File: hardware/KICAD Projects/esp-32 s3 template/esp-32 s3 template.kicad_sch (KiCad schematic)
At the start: 39 parts, among them J1 TYPE-C-31-M-12, J2 DTF13-6P, SW1 PTS810_SJM_250_SMTR_LFS, SW2 PTS810_SJM_250_SMTR_LFS, U1 AMS1117-3.3, U2 ESP32-S3-WROOM-1, U3 MCP2515-I, U4 TJA1050DRG, X1 ${ALTIUM_VALUE}

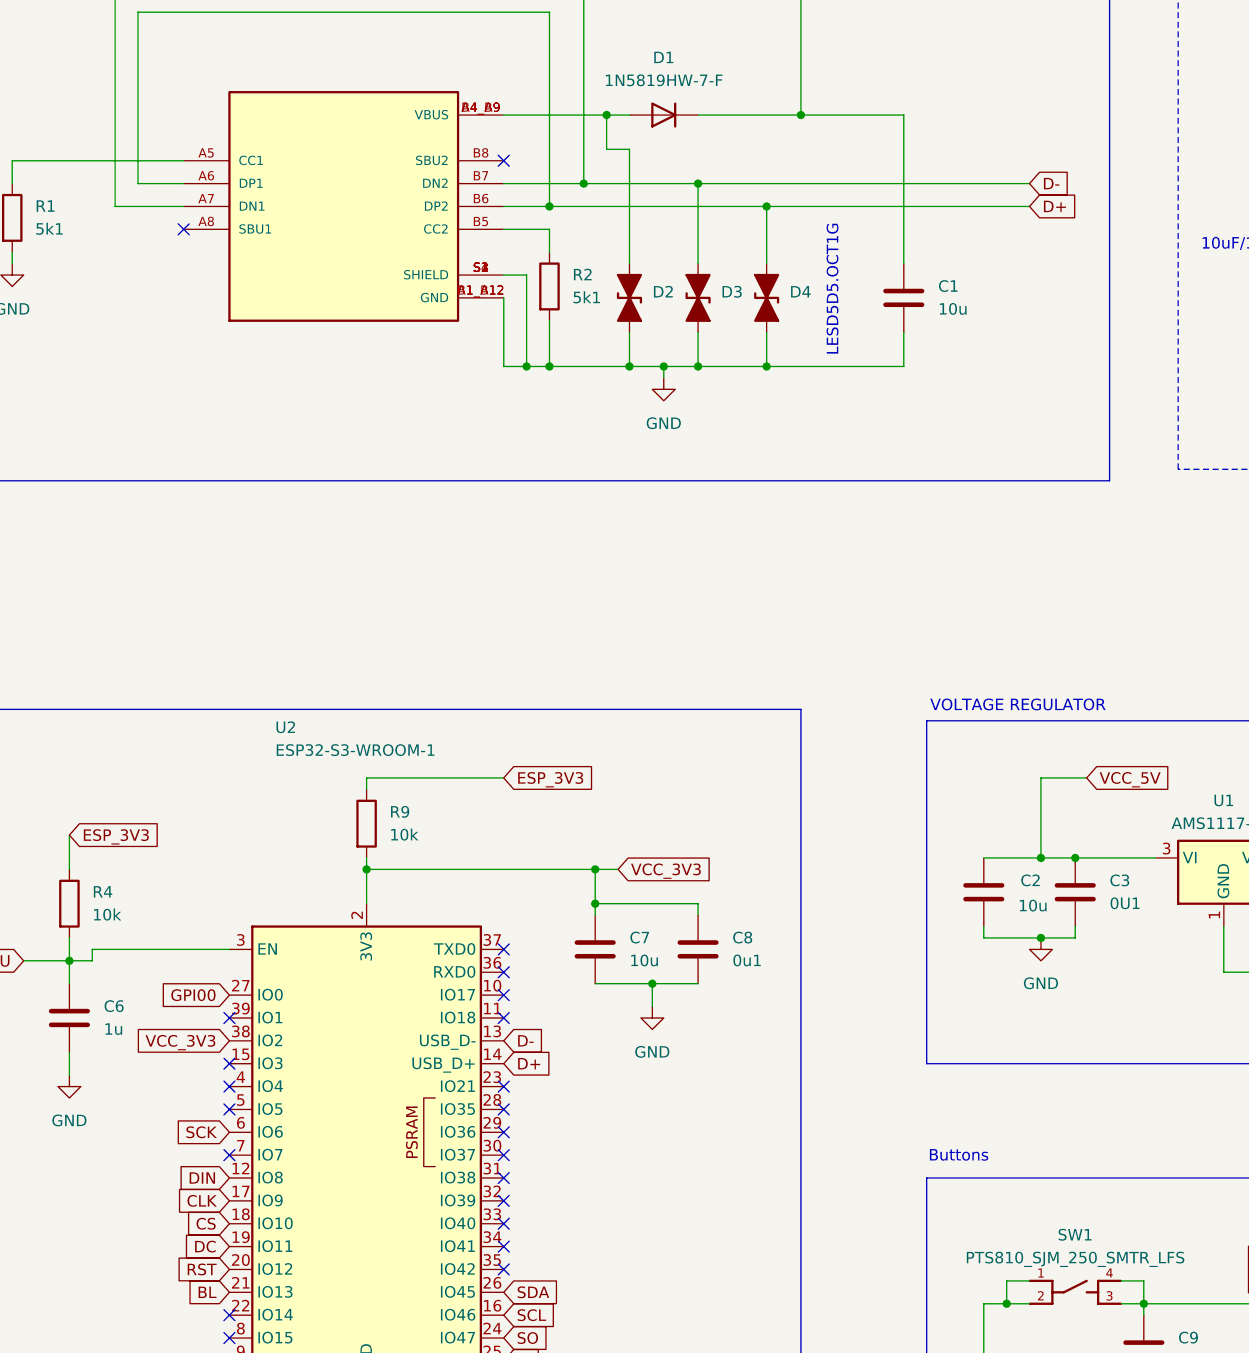
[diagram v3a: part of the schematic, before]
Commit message: everything but the ground fill
done, having some trouble with the ground fills
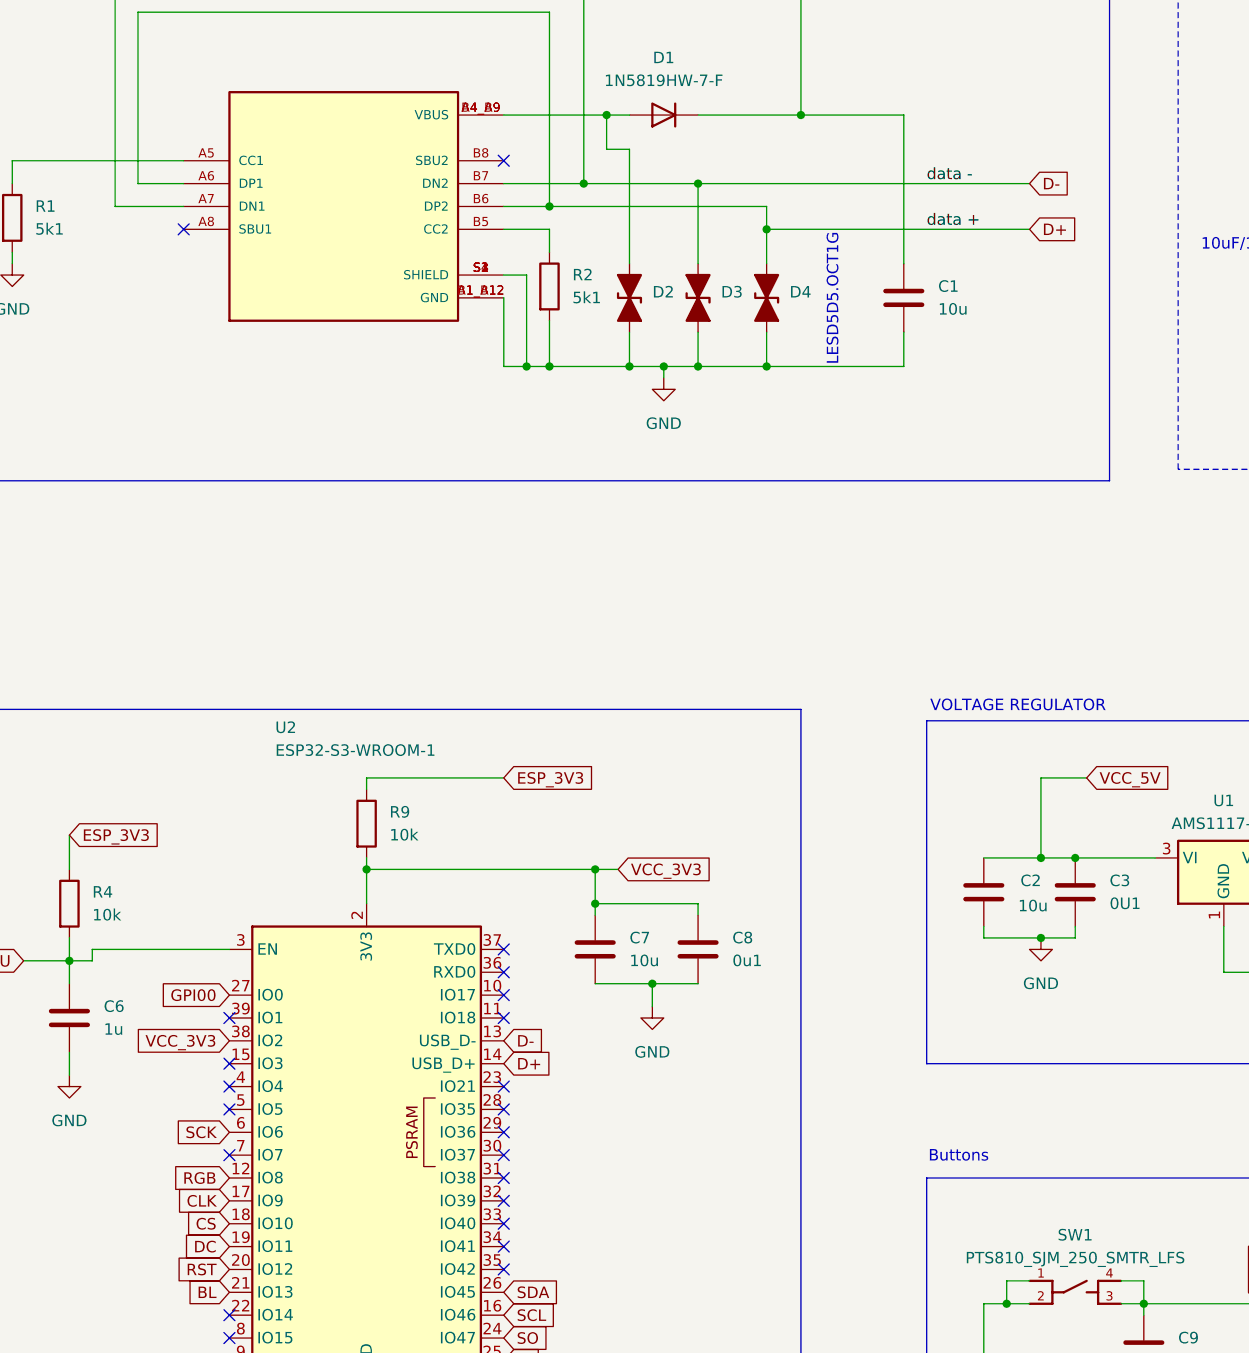
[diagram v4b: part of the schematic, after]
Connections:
- net DIN is gone; now on net RGB: U2.12 (IO8)
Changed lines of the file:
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@@
 	(text "LESD5D5.OCT1G"
 		(exclude_from_sim no)
-		(at 149.606 79.248 90)
+		(at 149.606 80.264 90)
 		(effects
 			(font
@@
 	)
 	(junction
-		(at 142.24 69.85)
-		(diameter 0)
-		(color 0 0 0 0)
-	)
-	(junction
 		(at 121.92 67.31)
 		(diameter 0)
@@
 	)
 	(junction
+		(at 142.24 72.39)
+		(diameter 0)
+		(color 0 0 0 0)
+	)
+	(junction
 		(at 123.19 147.32)
 		(diameter 0)
@@
 	(wire
 		(pts
-			(xy 142.24 69.85) (xy 171.45 69.85)
+			(xy 142.24 72.39) (xy 171.45 72.39)
 		)
 		(stroke
@@
 	(wire
 		(pts
+			(xy 142.24 72.39) (xy 142.24 76.2)
+		)
+		(stroke
+			(width 0)
+			(type default)
+		)
+	)
+	(wire
+		(pts
 			(xy 228.6 189.23) (xy 226.06 189.23)
 		)
@@
 	(wire
 		(pts
+			(xy 142.24 72.39) (xy 142.24 69.85)
+		)
+		(stroke
+			(width 0)
+			(type default)
+		)
+	)
+	(wire
+		(pts
 			(xy 113.03 69.85) (xy 118.11 69.85)
 		)
@@
 	(wire
 		(pts
-			(xy 142.24 69.85) (xy 142.24 76.2)
-		)
-		(stroke
-			(width 0)
-			(type default)
-		)
-	)
-	(wire
-		(pts
 			(xy 294.64 86.36) (xy 294.64 77.47)
 		)
@@
 			"MwA0ADkARQAtADMAMABDADMALQA0AEYAMQA1AC0AOQAxADIARgAtADEANwA0AEUARAA2AEUAMABD"
 			"ADYARQBGAIJIARj//////////4JTA08RIAAAAAAAAAAAAAAAAAAAAAAAAAAAAAAAAAAAAAAAAAAA"
+			"AAAAAAAAAAAAAAAAAAAAAAAAAAAAAAAAAAAAAAAAAAAAAAAAAAQAAG8BAAAAAAAAAAAAAAAAAAAA"
+			"AAAAAAAAAAAAAACDAAAAGAEAAPUDAABnAQAAAAAAAAAAAAAAAAAAAAAAAAAAAAAAAAAAAAAAAAAA"
+			"AAAAAAAAAAAAAAAAAAAAAAAAAAAAAAAAAAAAAAAAAAAAAAAAAAAAAAAAYAAAAAoBAAAAAAAAAAAA"
+			"AAAAAAAAAAAAAAAAAAAAAAAAAAAAAAAAAAAAAAAAAAAAAAAAAAAAAAAAAAAAAAAAAAAAAAAAAAAA"
+			"AAAAAAAAAAAAAAAAAAAAAIMDAABWAQAAAAAAAAAAAAA5AAAAewAAAAAAAAAAAAAAAAAAAAAAAAAA"
+			"AAAAAAAAAAAAAAAAAAAAAAAAAAAAAAAAAAAAAAAAAAAAAAAAAAAAAAAAAAAAAAAAAAAAAAAAAAAA"
+			"AAAAAAAAAAAAAAAAAAAAAAAAAAAAAAAAAAAAAAAAAAAAAAAAAAAAAAAAAAAAAAAAAAAAAAAAAAAA"
+			"AAAAAAAAAAAAAAAAAAAAAAAAAAAAAAAAAAAAAAAAAAAAAAAAAAAAAAAAAAAAAAAAAAAAAAAAAAAA"
+			"AAAAABkAAAAoAAAAAAAAAAAAAAAAAAAAAAAAAAAAAAAAAAAAAAAAAAAAAAAAAAAAAAAAAAAAAAAA"
+			"AAAAAAAAAAAAAAAAAAAAAAAAAAAAAAAAAAAAAAAAAAAAAAAAAAAAAAAAAAAAAAAAAAAAAAAAAAAA"
+			"AAAAAAAAAAAAAAAAAAAAAAAAAAAAAAAAAAAAAAAAAAAAAAAAAAAAAAAAAAAAAAAAAAAAAAAAAAAA"
+			"AAAAAAAAAAAAAAAAAAAAAAAAAAAAAAAAAAAAAAAAAAAAAAAAAAAAAAAAAAAAAAAAAA8BAAAnAQAA"
+			"AAAAAAAAAAAAAAAAAAAAAAAAAAAAAAAAAAAAAAAAAAAAAAAAAAAAAAAAAAAAAAAAAAAAAAAAAAAA"
+			"AAAAAAAAAAAAAAAAAAAAAAAAAAAAAAAAAAAAAAAAAAAAAAAAAAAAAAAAAAAAAAAAAAAAAAAAAAAA"
+			"AAAAAAAAIQAAAD0AAAAAAAAAAAAAAAAAAAAAAAAAAAAAAAAAAAAAAAAAAAAAAAAAAAAAAAAAAAAA"
+			"AAAAAAAAAAAAAAAAAAAAAAAAAAAAAAAAAAAAAAAAAAAAAAAAAAAAAAAAAAAAAAAAAAAAAAAAAAAA"
+			"AAAAAAAAAAAAAAAAPwQAAG4BAAAAAAAAAAAAAAAAAAAAAAAAAAAAAAAAAAAAAAAAAAAAAAAAAAAA"
+			"AAAAAAAAAAAAAAAAAAAAAAAAAAAAAAAAAAAAAAAAAAAAAAAAAAAAAAAAAAAAAAAAAAAAAAAAAAAA"
+			"AAAAAAAAAAAAAAAAAAAAAAAAAAAAAAAAAAAAAAAAAAAAALQAAAAAAAAAAAAAAAAAAAAAAAAAAAAA"
+			"AAAAAAAAAAAAAAAAAAAAAAAAAAAAAAAAAAAAAAAAAAAAAAAAAAAAAAAAAAAAAAAAAAAAAAAAAAAA"
+			"AAAAAAAAAAAAAAAAAAAAAAAAAAAAAAAAAAAAAAAAAAAAAAAAAAAAAAAAAAAAAAAAAAAAAAAAAAAA"
+			"AAAAAAAAAAAAAAAAAAAAAAAAAAAAAAAAAAAAAAAAAAAAAAAAAAAAAAAAAAAAAAAAAAAAAAAAAAAA"
+			"AAAAAAAAAAAAAAAAAAAAAAAAAAAAAAAAAAAAAAAAAAAAAAAAAAAAAAAAAAAAAAAAAAAAAAAAAAAA"
+			"AAAAAAAAAAAAAAAAAAAAAAAAAAAAAAAAAAAAAAAAAAAAAAAAAAAAAAAAAAAAAAAAAAAAAAAAAAAA"
+			"AAAAAAAAAAAAAAAAAAAAAAAAAAAAAAAAAAAAAAAAAAAAAAAAAAAAAAAAAAAAAAAAAAAAAAAAAAAA"
+			"AAAAAAAAAAAAAAAAAAAAAAAAAAAAAAAAAAAAAAAAAAAAAAAAAAAAAAAAAAAAAAAAAAAAAAAAAAAA"
+			"AAAAAAAAAAAAAAAAAAAAAAAAAAAAAAAAAAAAAAAAAAAAAAAAAAAAAAAAAAAAAAAAAAAAAAAAAAAA"
+			"AAAAAAAAAAAAAAAAAAAAAAAAAAAAAAAAAAAAAAAAAAAAAAAAAAAAAAAAAAAAAAAAAAAAAAAAAAAA"
+			"AAAAAAAAAAAAAAAAAAAAAAAAAAAAAAAAAAAAAAAAAAAAAAAAAAAAAAAAAAAAAAAAAAAAAAAAAAAA"
+			"AAAAAAAAAAAAAAAAAAAAAAAAAAAAAAAAAAAAAAAAAAAAAAAAAAAAAAAAAAAAAAAAAAAAAAAAAAAA"
+			"AAAAAAAAAAAAAAAAAAAAAAAAAAAAAAAAAAAAAAAAAAAAAAAAAAAAAAAAAAAAAAAAAAAAAAAAAAAA"
+			"AAAAAAAAAAAAAAAAAAAAAAAAAAAAAAAAAAAAAAAAAAAAAAAAAAAAAAAAAAAAAAAAAAAAAAAAAAAA"
+			"AAAAAAAAAAAAAAAAAAAAAAAAAAAAAAAAAAAAAAAAAAAAAAAAAAAAAAAAAAAAAAAAAAAAAAAAAAAA"
+			"AAAAAAAAAAAAAAAAAAAAAAAAAAAAAAAAAAAAAAAAAAAAAAAAAAAAAAAAAAAAAAAAAAAAAAAAAAAA"
+			"AAAAAAAAAAAAAAAAAAAAAAAAAAAAAAAAAAAAAAAAAAAAAAAAAAAAAAAAAAAAAAAAAAAAAAAAAAAA"
+			"AAAAAAAAAAAAAAAAAAAAAAAAAAAAAAAAAAAAAAAAAAAAAAAAAAAAAAAAAAAAAAAAAAAAAAAAAAAA"
 			"AAAAAAAAAAAAAAAAAAAAAAAAAAAAAAAAAAAAAAAAAAAAAAAAAA=="
 		)
 	)
+	(label "data -"
+		(at 160.02 67.31 0)
+		(fields_autoplaced yes)
+		(effects
+			(font
+				(size 1.27 1.27)
+			)
+			(justify left bottom)
+		)
+		(property "Netclass" "usb_c"
+			(at 160.02 68.58 0)
+			(effects
+				(font
+					(size 1.27 1.27)
+					(italic yes)
+				)
+				(justify left)
+			)
+		)
+	)
+	(label "data +"
+		(at 160.02 72.39 0)
+		(fields_autoplaced yes)
+		(effects
+			(font
+				(size 1.27 1.27)
+			)
+			(justify left bottom)
+		)
+		(property "Netclass" "usb_c"
+			(at 160.02 73.66 0)
+			(effects
+				(font
+					(size 1.27 1.27)
+					(italic yes)
+				)
+				(justify left)
+			)
+		)
+	)
 	(global_label "High"
 		(shape input)
@@
 		)
 	)
-	(global_label "DIN"
+	(global_label "RGB"
 		(shape input)
 		(at 82.55 177.8 180)
@@
 		)
 		(property "Intersheetrefs" "${INTERSHEET_REFS}"
-			(at 76.3595 177.8 0)
+			(at 75.7548 177.8 0)
 			(effects
 				(font
@@
 	(global_label "D+"
 		(shape input)
-		(at 171.45 69.85 0)
+		(at 171.45 72.39 0)
 		(fields_autoplaced yes)
 		(effects
@@
 		)
 		(property "Intersheetrefs" "${INTERSHEET_REFS}"
-			(at 177.2776 69.85 0)
+			(at 177.2776 72.39 0)
 			(effects
 				(font
